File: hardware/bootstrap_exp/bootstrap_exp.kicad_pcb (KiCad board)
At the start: 4 copper layers, 45.7 x 35.6 mm, 32 parts, among them J1 Conn_Coaxial, J2 Conn_Coaxial, U1 OPA810DBV, U2 OPA810DBV, U3 OPA810DBV, U4 OPA810DBV

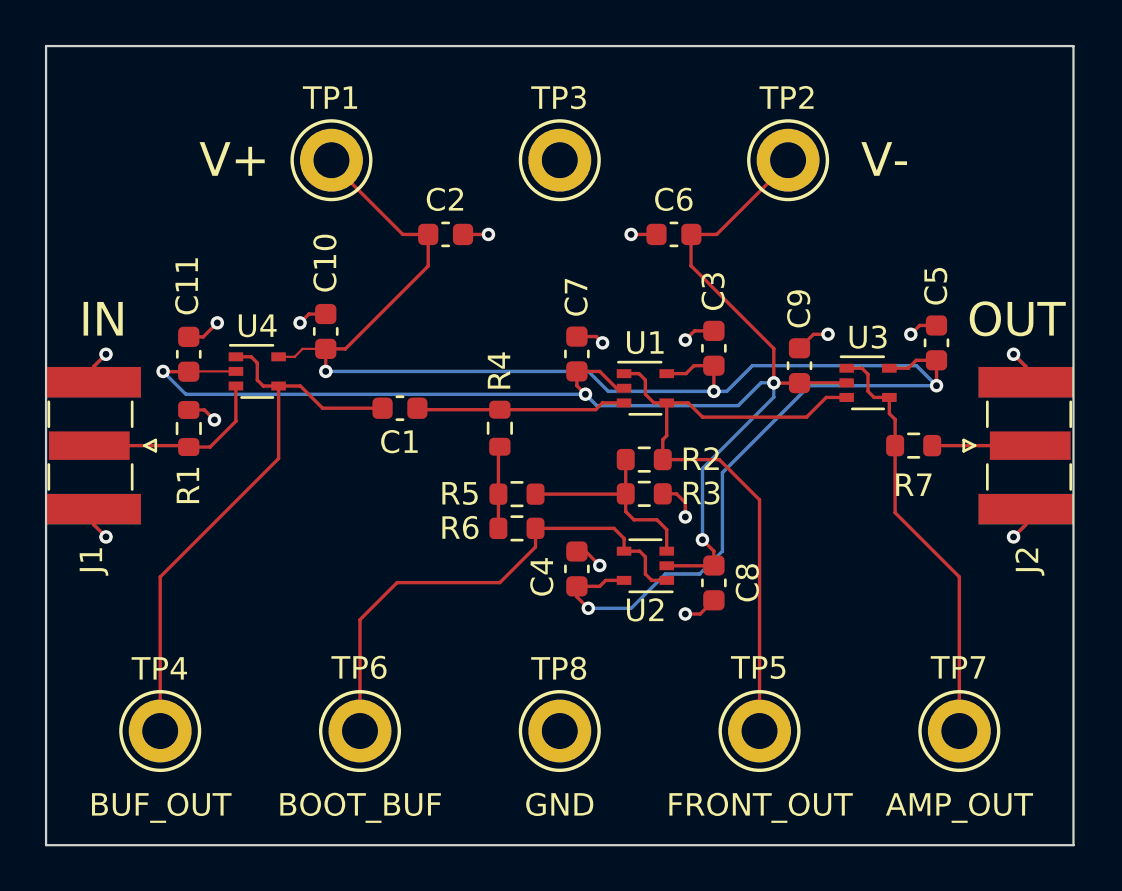
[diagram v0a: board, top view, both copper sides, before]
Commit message: Move SMA connectors to fix edge clearance violations
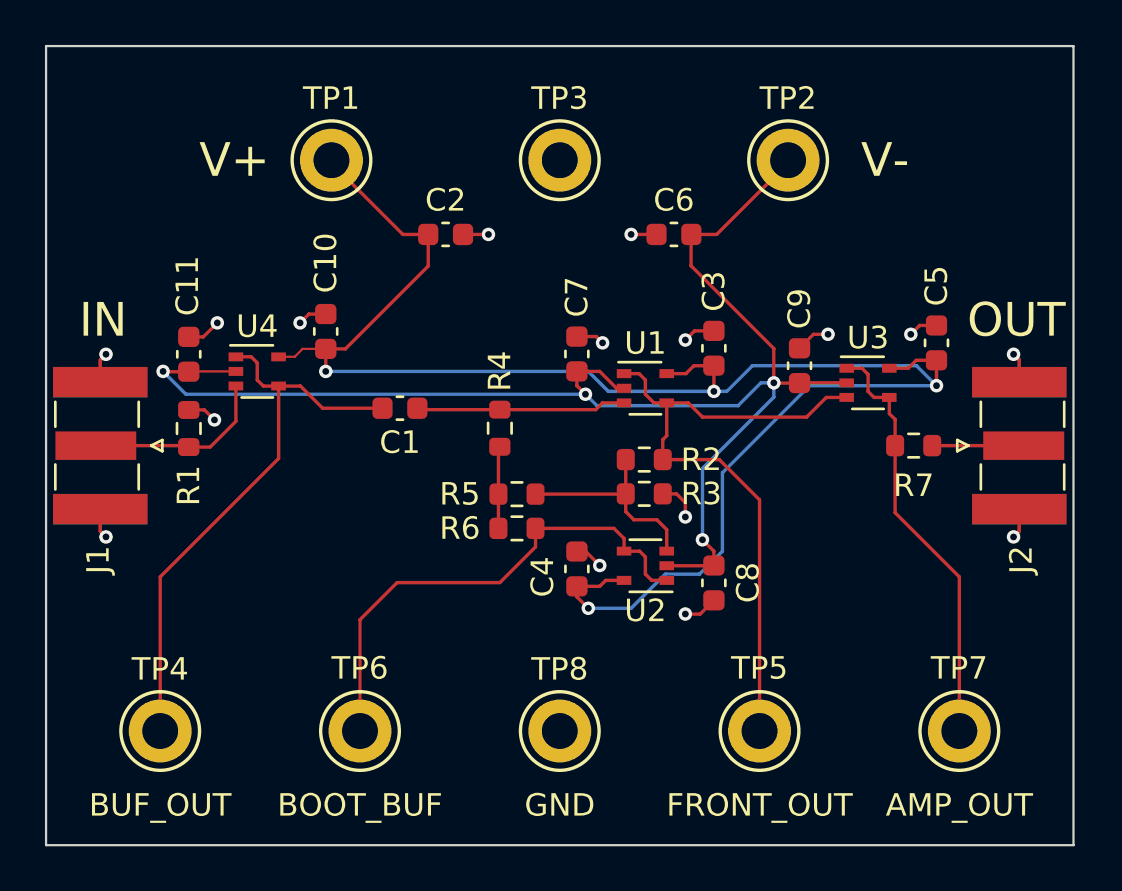
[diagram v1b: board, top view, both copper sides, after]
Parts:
- moved J1 0.29 mm to (114.2, 96.5)
- moved J2 0.29 mm to (155.1, 96.5)
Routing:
- net GND: track 28.3 -> 27.3 mm
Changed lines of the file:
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@@
   )
   (footprint "Connector_Coaxial:SMA_Samtec_SMA-J-P-X-ST-EM1_EdgeMount" (layer "F.Cu")
-    (at 155.3575 96.52 90)
+    (at 155.067 96.52 90)
     (descr "Connector SMA, 0Hz to 20GHz, 50Ohm, Edge Mount (http://suddendocs.samtec.com/prints/sma-j-p-x-st-em1-mkt.pdf)")
     (tags "SMA Straight Samtec Edge Mount")
@@
   )
   (footprint "Connector_Coaxial:SMA_Samtec_SMA-J-P-X-ST-EM1_EdgeMount" (layer "F.Cu")
-    (at 113.8825 96.52 -90)
+    (at 114.173 96.52 -90)
     (descr "Connector SMA, 0Hz to 20GHz, 50Ohm, Edge Mount (http://suddendocs.samtec.com/prints/sma-j-p-x-st-em1-mkt.pdf)")
     (tags "SMA Straight Samtec Edge Mount")
@@
   (segment (start 141.859 101.219) (end 141.859 97.7265) (width 0.15) (layer "B.Cu") (net 2))
   (segment (start 141.478 103.404) (end 140.869 104.013) (width 0.15) (layer "F.Cu") (net 3))
+  (segment (start 114.173 100.33) (end 114.427 100.584) (width 0.15) (layer "F.Cu") (net 3))
   (segment (start 150.635 91.173) (end 150.241 91.567) (width 0.15) (layer "F.Cu") (net 3))
-  (segment (start 155.3575 100.0395) (end 154.813 100.584) (width 0.15) (layer "F.Cu") (net 3))
+  (segment (start 114.173 93.695) (end 114.173 92.71) (width 0.15) (layer "F.Cu") (net 3))
+  (segment (start 155.067 100.33) (end 154.813 100.584) (width 0.15) (layer "F.Cu") (net 3))
   (segment (start 140.208 99.695) (end 140.208 99.06) (width 0.15) (layer "F.Cu") (net 3))
-  (segment (start 155.3575 93.695) (end 155.3575 93.0005) (width 0.15) (layer "F.Cu") (net 3))
-  (segment (start 155.3575 99.345) (end 155.3575 100.0395) (width 0.15) (layer "F.Cu") (net 3))
   (segment (start 118.809 94.933) (end 119.253 95.377) (width 0.15) (layer "F.Cu") (net 3))
-  (segment (start 113.8825 100.0395) (end 114.427 100.584) (width 0.15) (layer "F.Cu") (net 3))
   (segment (start 141.478 91.414) (end 140.615 91.414) (width 0.15) (layer "F.Cu") (net 3))
   (segment (start 138.925 87.122) (end 137.795 87.122) (width 0.15) (layer "F.Cu") (net 3))
+  (segment (start 114.173 99.345) (end 114.173 100.33) (width 0.15) (layer "F.Cu") (net 3))
+  (segment (start 155.067 93.695) (end 155.067 92.71) (width 0.15) (layer "F.Cu") (net 3))
   (segment (start 151.384 91.173) (end 150.635 91.173) (width 0.15) (layer "F.Cu") (net 3))
-  (segment (start 113.8825 99.345) (end 113.8825 100.0395) (width 0.15) (layer "F.Cu") (net 3))
   (segment (start 135.382 91.668) (end 136.245 91.668) (width 0.15) (layer "F.Cu") (net 3))
   (segment (start 135.382 101.232) (end 135.776 101.232) (width 0.15) (layer "F.Cu") (net 3))
   (segment (start 118.11 91.681) (end 118.758 91.681) (width 0.15) (layer "F.Cu") (net 3))
   (segment (start 130.315 87.122) (end 131.445 87.122) (width 0.15) (layer "F.Cu") (net 3))
-  (segment (start 155.3575 93.0005) (end 154.813 92.456) (width 0.15) (layer "F.Cu") (net 3))
+  (segment (start 114.173 92.71) (end 114.427 92.456) (width 0.15) (layer "F.Cu") (net 3))
   (segment (start 140.615 91.414) (end 140.208 91.821) (width 0.15) (layer "F.Cu") (net 3))
   (segment (start 118.758 91.681) (end 119.38 91.059) (width 0.15) (layer "F.Cu") (net 3))
   (segment (start 123.063 91.059) (end 123.457 90.665) (width 0.15) (layer "F.Cu") (net 3))
+  (segment (start 155.067 92.71) (end 154.813 92.456) (width 0.15) (layer "F.Cu") (net 3))
   (segment (start 145.288 92.189) (end 145.91 91.567) (width 0.15) (layer "F.Cu") (net 3))
-  (segment (start 113.8825 93.695) (end 113.8825 93.0005) (width 0.15) (layer "F.Cu") (net 3))
-  (segment (start 113.8825 93.0005) (end 114.427 92.456) (width 0.15) (layer "F.Cu") (net 3))
   (segment (start 118.11 94.933) (end 118.809 94.933) (width 0.15) (layer "F.Cu") (net 3))
   (segment (start 140.208 99.06) (end 139.814 98.666) (width 0.15) (layer "F.Cu") (net 3))
   (segment (start 136.245 91.668) (end 136.525 91.948) (width 0.15) (layer "F.Cu") (net 3))
   (segment (start 145.91 91.567) (end 146.558 91.567) (width 0.15) (layer "F.Cu") (net 3))
+  (segment (start 155.067 99.345) (end 155.067 100.33) (width 0.15) (layer "F.Cu") (net 3))
   (segment (start 140.869 104.013) (end 140.208 104.013) (width 0.15) (layer "F.Cu") (net 3))
   (segment (start 135.776 101.232) (end 136.398 101.854) (width 0.15) (layer "F.Cu") (net 3))
@@
   (via (at 136.525 91.948) (size 0.6) (drill 0.3) (layers "F.Cu" "B.Cu") (net 3))
   (via (at 114.427 100.584) (size 0.6) (drill 0.3) (layers "F.Cu" "B.Cu") (net 3))
-  (segment (start 155.3575 100.0395) (end 154.813 100.584) (width 0.15) (layer "B.Cu") (net 3))
-  (segment (start 155.3575 93.695) (end 155.3575 93.0005) (width 0.15) (layer "B.Cu") (net 3))
-  (segment (start 155.3575 93.0005) (end 154.813 92.456) (width 0.15) (layer "B.Cu") (net 3))
-  (segment (start 113.8825 99.345) (end 113.8825 100.0395) (width 0.15) (layer "B.Cu") (net 3))
-  (segment (start 113.8825 100.0395) (end 114.427 100.584) (width 0.15) (layer "B.Cu") (net 3))
-  (segment (start 155.3575 99.345) (end 155.3575 100.0395) (width 0.15) (layer "B.Cu") (net 3))
-  (segment (start 113.8825 93.695) (end 113.8825 93.0005) (width 0.15) (layer "B.Cu") (net 3))
-  (segment (start 113.8825 93.0005) (end 114.427 92.456) (width 0.15) (layer "B.Cu") (net 3))
+  (segment (start 114.173 92.71) (end 114.427 92.456) (width 0.15) (layer "B.Cu") (net 3))
+  (segment (start 114.173 100.33) (end 114.427 100.584) (width 0.15) (layer "B.Cu") (net 3))
+  (segment (start 155.067 100.33) (end 154.813 100.584) (width 0.15) (layer "B.Cu") (net 3))
+  (segment (start 155.067 92.71) (end 154.813 92.456) (width 0.15) (layer "B.Cu") (net 3))
+  (segment (start 155.067 93.695) (end 155.067 92.71) (width 0.15) (layer "B.Cu") (net 3))
+  (segment (start 155.067 99.345) (end 155.067 100.33) (width 0.15) (layer "B.Cu") (net 3))
+  (segment (start 114.173 93.695) (end 114.173 92.71) (width 0.15) (layer "B.Cu") (net 3))
+  (segment (start 114.173 99.345) (end 114.173 100.33) (width 0.15) (layer "B.Cu") (net 3))
   (segment (start 136.398 93.218) (end 135.382 93.218) (width 0.15) (layer "F.Cu") (net 4))
   (segment (start 141.478 101.854) (end 141.478 101.219) (width 0.15) (layer "F.Cu") (net 4))
@@
   (segment (start 128.347 94.92) (end 131.953 94.92) (width 0.15) (layer "F.Cu") (net 5))
   (segment (start 131.953 94.92) (end 136.22 94.92) (width 0.15) (layer "F.Cu") (net 5))
-  (segment (start 151.193 96.52) (end 155.5575 96.52) (width 0.15) (layer "F.Cu") (net 6))
+  (segment (start 151.193 96.52) (end 155.267 96.52) (width 0.15) (layer "F.Cu") (net 6))
   (segment (start 140.337 94.617) (end 140.97 95.25) (width 0.15) (layer "F.Cu") (net 7))
   (segment (start 145.6055 95.25) (end 146.4795 94.376) (width 0.15) (layer "F.Cu") (net 7))
@@
   (segment (start 152.4 102.362) (end 149.543 99.505) (width 0.15) (layer "F.Cu") (net 11))
   (segment (start 120.208 95.438) (end 120.208 93.868) (width 0.15) (layer "F.Cu") (net 12))
-  (segment (start 113.6825 96.52) (end 118.047 96.52) (width 0.15) (layer "F.Cu") (net 12))
+  (segment (start 118.047 96.52) (end 118.11 96.583) (width 0.15) (layer "F.Cu") (net 12))
   (segment (start 118.11 96.583) (end 119.063 96.583) (width 0.15) (layer "F.Cu") (net 12))
+  (segment (start 113.973 96.52) (end 118.047 96.52) (width 0.15) (layer "F.Cu") (net 12))
   (segment (start 119.063 96.583) (end 120.208 95.438) (width 0.15) (layer "F.Cu") (net 12))
-  (segment (start 118.047 96.52) (end 118.11 96.583) (width 0.15) (layer "F.Cu") (net 12))
   (zone (net 3) (net_name "GND") (layers "In1.Cu" "In2.Cu") (hatch edge 0.508)
     (connect_pads (clearance 0.508))

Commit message: Specify MPN and source for every component
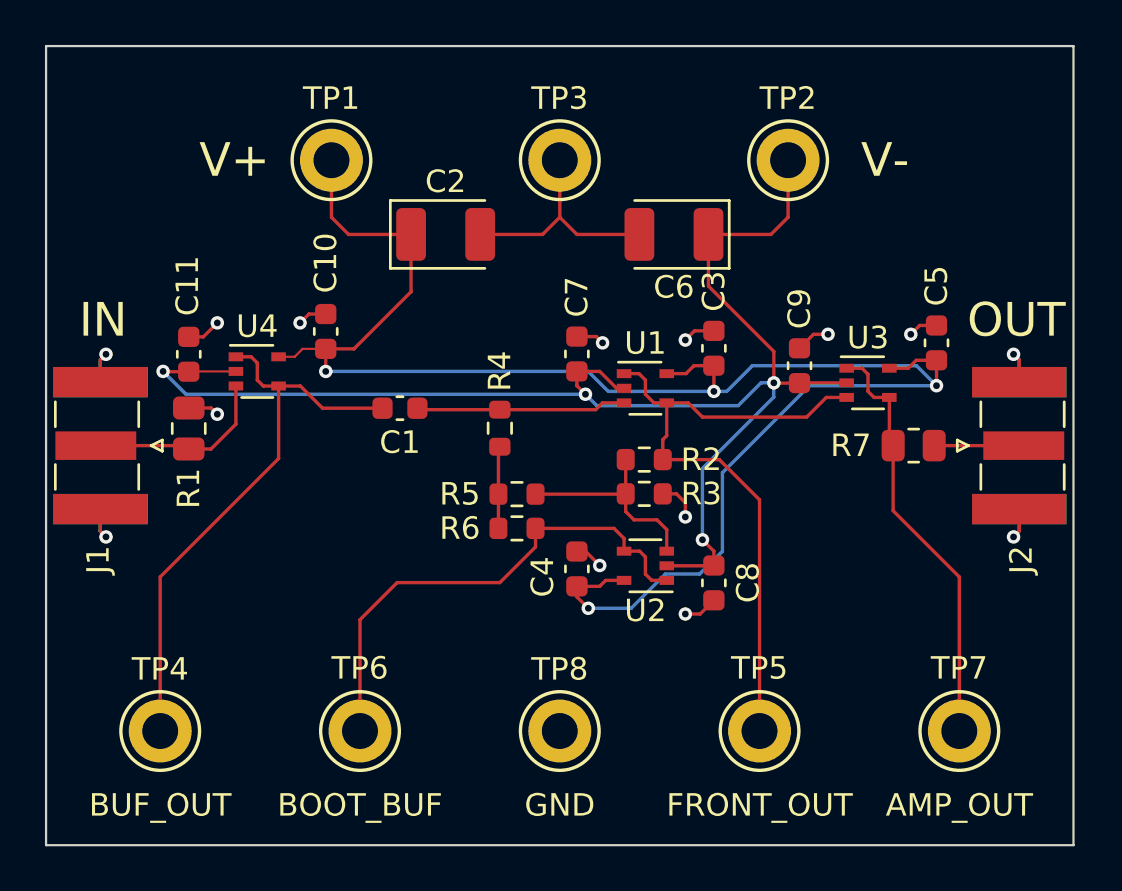
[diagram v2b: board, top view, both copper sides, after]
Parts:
- C1: value 80p/C0G -> 100p/NP0/1%
- C2, C6: footprint Capacitor_SMD:C_0603_1608Metric -> Capacitor_Tantalum_SMD:CP_EIA-3528-12_Kemet-T
- R1, R7: footprint Resistor_SMD:R_0603_1608Metric -> Resistor_SMD:R_0805_2012Metric
- U1, U2, U3, U4: value OPA810DBV -> OPA810
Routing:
- net GND: track 27.3 -> 35.4 mm, vias 16 -> 14
- net /V+: track 76.7 -> 77.2 mm
